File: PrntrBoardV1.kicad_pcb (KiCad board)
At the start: 4 copper layers, 99 x 99 mm, 234 parts, among them J1 EXT 5V, J10 Probe, J11 Extruder Heater, J12 Stepper, J13 Thermistor, J14 Max, J15 Min, J16 Max, J17 Min, J18 Max, J19 Min, J2 Bed Heater, J20 Stepper, J21 Stepper, J22 Stepper, J23 Stepper, J24 Probe, J25 Extruder Heater, J26 Stepper, J27 Thermistor, J28 Thermistor, J29 12-24V, J3 Z Probe, J30 LCD, J31 TC1, J32 TC2, J4 E0 Cool, J5 E0 Part, J6 E1 Cool, J7 E1 Part, J8 Always On Fan 1, J9 Always On Fan 2, U1 4078, U11 NUCLEO-64, U2 74HCT02, U3 74LVC125, U4 TMC5130, U5 TMC5130, U6 TMC5130, U7 TMC5130, U8 TMC5130, X1 16MHz

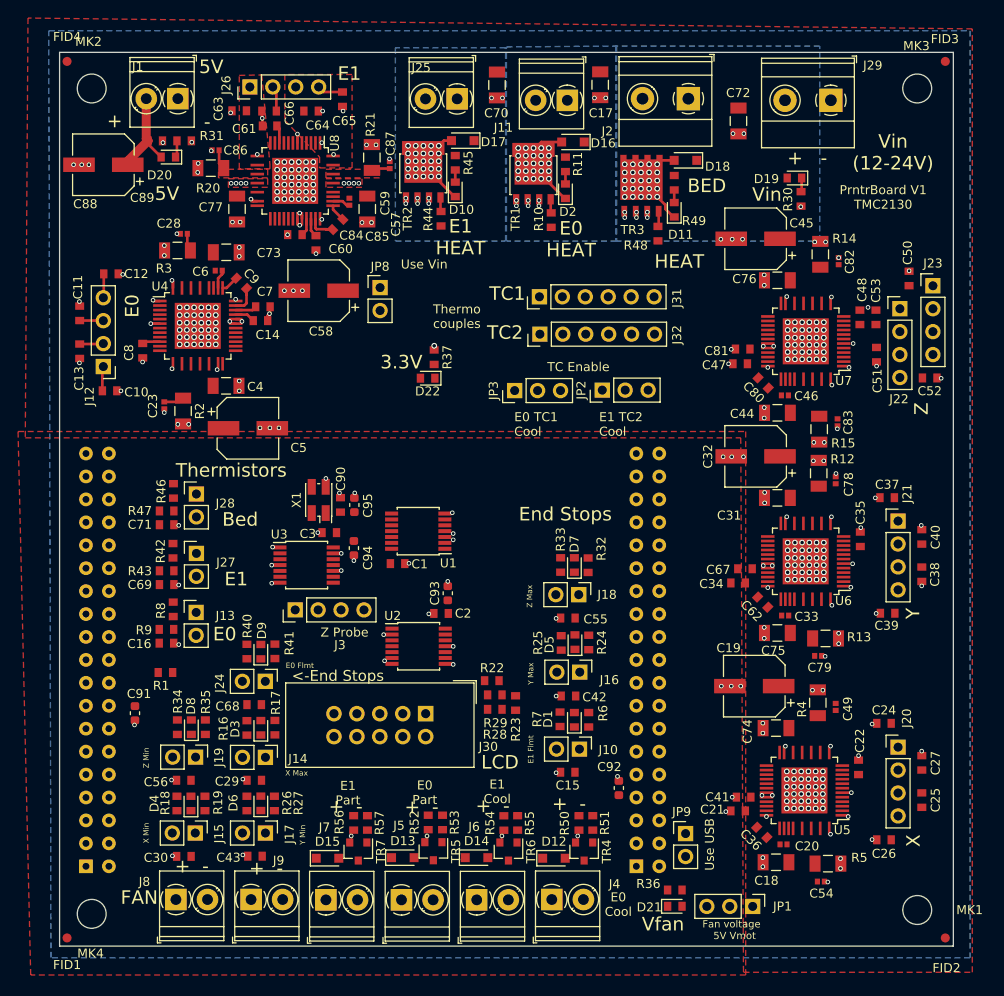
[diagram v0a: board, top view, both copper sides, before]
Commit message: Fix endstops. Add extra fan connectors. Start routing motors drivers.
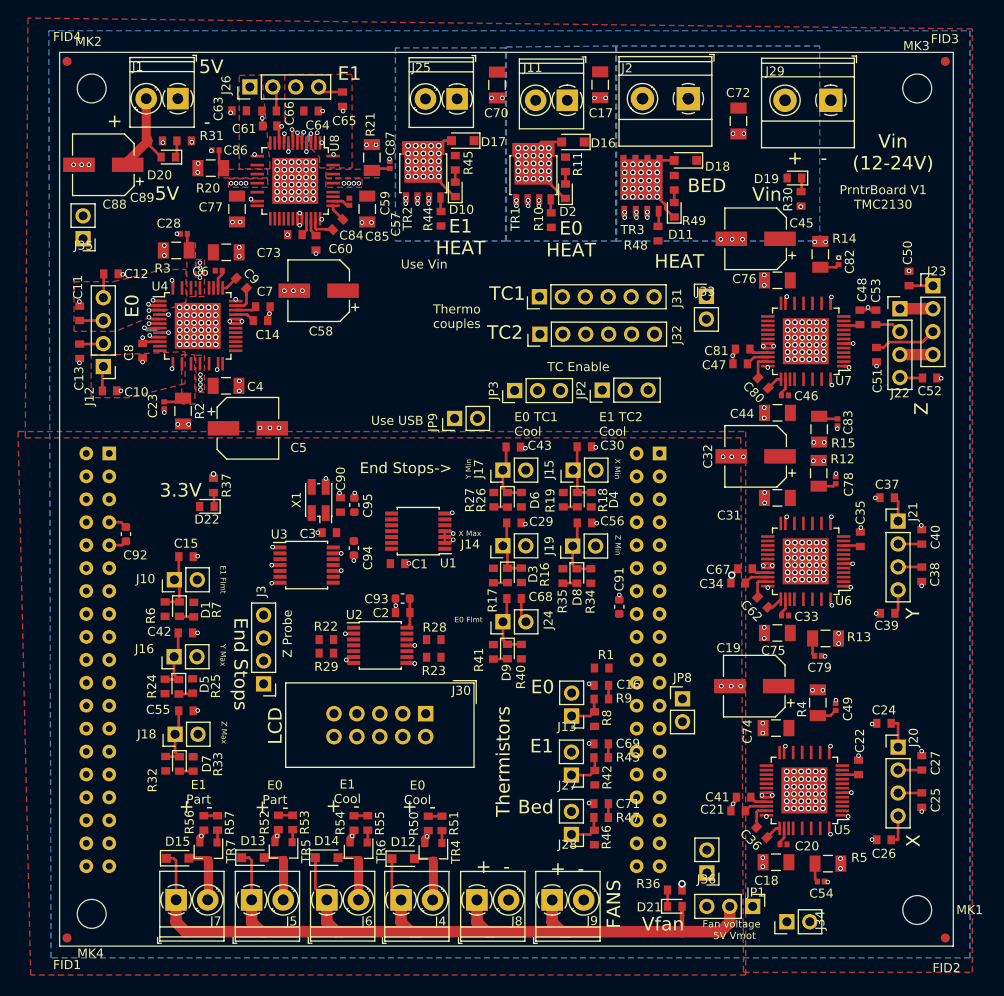
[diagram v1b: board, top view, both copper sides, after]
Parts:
- added J33: Vin, Connector_PinHeader_2.54mm:PinHeader_1x02_P2.54mm_Vertical, F.Cu at (91.7, 46.0)
- added J34: Vin, Connector_PinHeader_2.54mm:PinHeader_1x02_P2.54mm_Vertical, F.Cu at (100.6, 115.3)
- added J35: 5V, Connector_PinHeader_2.54mm:PinHeader_1x02_P2.54mm_Vertical, F.Cu at (22.6, 39.6)
- added J36: 5V, Connector_PinHeader_2.54mm:PinHeader_1x02_P2.54mm_Vertical, F.Cu at (91.7, 109.9)
- moved U11 78.3 mm to (86.5, 109.2), turned to 180 degrees
- moved C30 63.5 mm to (78.1, 62.7), turned to 0 degrees
- moved C92 61.4 mm to (27.4, 72.4), turned to 270 degrees
- moved R46 60.4 mm to (79.2, 106.0), turned to 90 degrees
- moved R47 58.9 mm to (80.0, 103.8), turned to 180 degrees
- moved J15 58.0 mm to (76.9, 65.3), turned to 90 degrees
- moved C71 57.2 mm to (80.0, 102.2), turned to 180 degrees
- moved R18 56.9 mm to (78.9, 68.5), turned to 90 degrees
- moved JP8 56.5 mm to (89.0, 90.6)
- moved J28 56.1 mm to (76.7, 105.6), turned to 180 degrees
- moved C91 54.9 mm to (82.0, 80.4), turned to 90 degrees
- moved D4 54.4 mm to (77.3, 68.5), turned to 270 degrees
- moved C43 53.6 mm to (70.3, 62.7), turned to 0 degrees
- moved R42 53.1 mm to (79.3, 99.3), turned to 90 degrees
- moved C56 52.8 mm to (78.1, 71.1), turned to 0 degrees
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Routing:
- net /E0 Cooling Fan/V_FAN: track 0.00 -> 114.2 mm
- net GND: track 14.9 -> 77.9 mm
- net /3.3V: track 3.98 -> 30.0 mm, vias 0 -> 2
- net /MISO: track 0.00 -> 23.8 mm, vias 0 -> 2
- net /MOSI_BUF: track 0.00 -> 20.7 mm, vias 0 -> 2
- net /MotorControl/E0/CLOCK: track 0.00 -> 19.6 mm, vias 0 -> 2
- net /SCK_BUF: track 0.00 -> 15.5 mm, vias 0 -> 2
- net /5V: track 15.2 -> 26.5 mm
- net /~E1_CS: track 0.00 -> 11.1 mm, vias 0 -> 1
- net /E0_DIR: track 0.00 -> 10.6 mm, vias 0 -> 1
- net /~E0_CS: track 0.00 -> 10.2 mm, vias 0 -> 1
- net /E1_DIR: track 0.00 -> 9.49 mm, vias 0 -> 1
- net /E1_STEP: track 0.00 -> 8.69 mm, vias 0 -> 1
- net /E0_STEP: track 0.00 -> 8.57 mm, vias 0 -> 1
- net /MotorControl/Y Axis/MaxStop/SENSOR: track 0.00 -> 7.12 mm
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- added copper zone on F.Cu, net /MotorControl/E0/Driver/MOTA1
- added copper zone on F.Cu, net /MotorControl/E0/Driver/MOTA2
- added copper zone on In2.Cu, net /MotorControl/E0/Driver/MOTA2
- added copper zone on F.Cu, net /MotorControl/E0/Driver/MOTB1
- added copper zone on F.Cu, net /MotorControl/E0/Driver/MOTB2
- added copper zone on In2.Cu, net /MotorControl/E0/Driver/MOTB2
- added copper zone on F.Cu, net Net-(C23-Pad1)
- added copper zone on F.Cu, net Net-(C28-Pad1)
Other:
- board text added: "End Stops->"
- board text added: "FANS"
- board text removed: "<-End Stops"
- board text removed: "FAN"

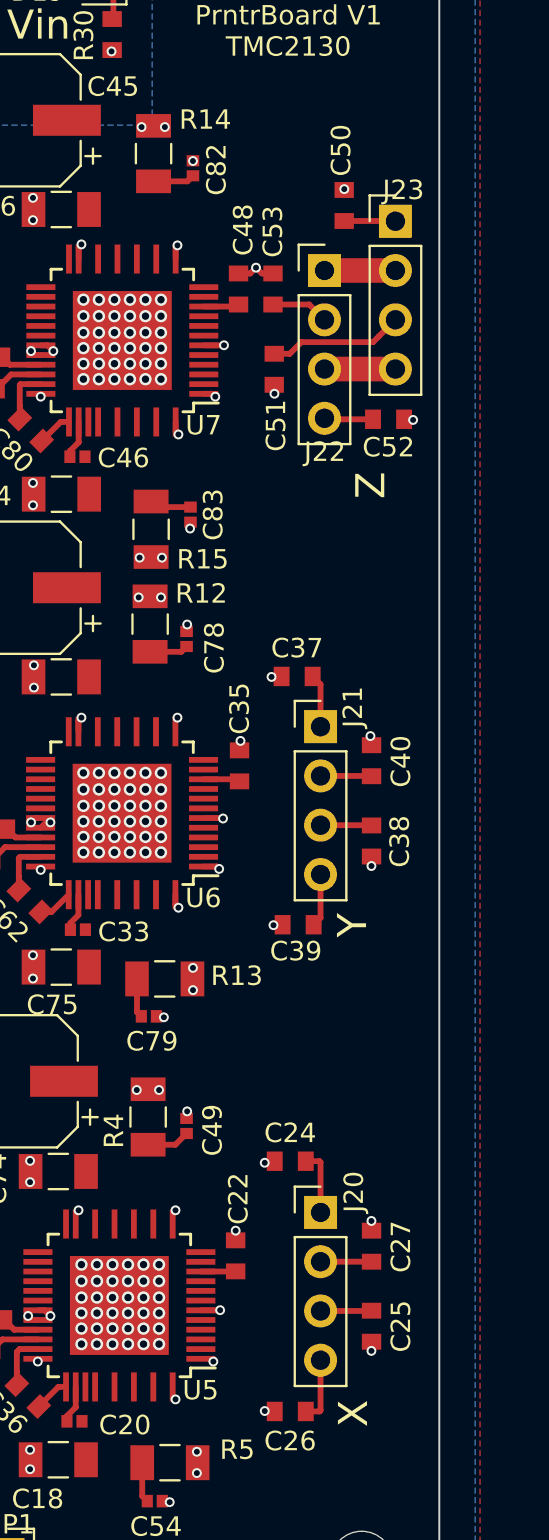
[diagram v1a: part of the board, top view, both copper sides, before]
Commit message: Added more motor power traces.
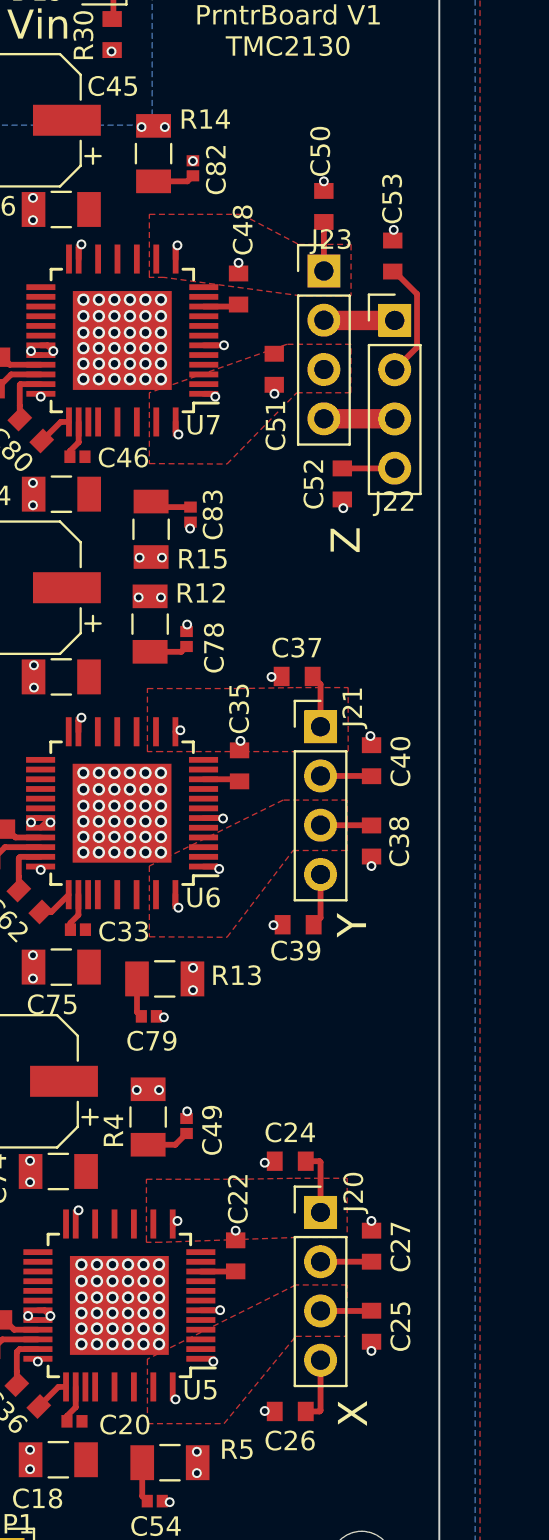
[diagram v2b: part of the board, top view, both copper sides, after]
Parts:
- moved C53 6.40 mm to (116.6, 46.6)
- moved J23 4.49 mm to (113.0, 47.4)
- moved J22 4.44 mm to (116.7, 50.0)
- moved C52 4.10 mm to (114.0, 58.4), turned to 90 degrees
- moved C50 1.05 mm to (113.0, 44.1)
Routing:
- net /MotorControl/Z Axis/MOTA1: track 6.97 -> 0.00 mm
- net /MotorControl/Z Axis/MOTB2: track 2.98 -> 6.11 mm
- net GND: track 77.9 -> 78.1 mm, vias 380 -> 381
- added copper zone on F.Cu, net /MotorControl/X Axis/MOTA1
- added copper zone on F.Cu, net /MotorControl/X Axis/MOTB1
- added copper zone on F.Cu, net /MotorControl/Y Axis/MOTA1
- added copper zone on F.Cu, net /MotorControl/Y Axis/MOTB1
- added copper zone on F.Cu, net /MotorControl/Z Axis/MOTA1
- added copper zone on F.Cu, net /MotorControl/Z Axis/MOTB1

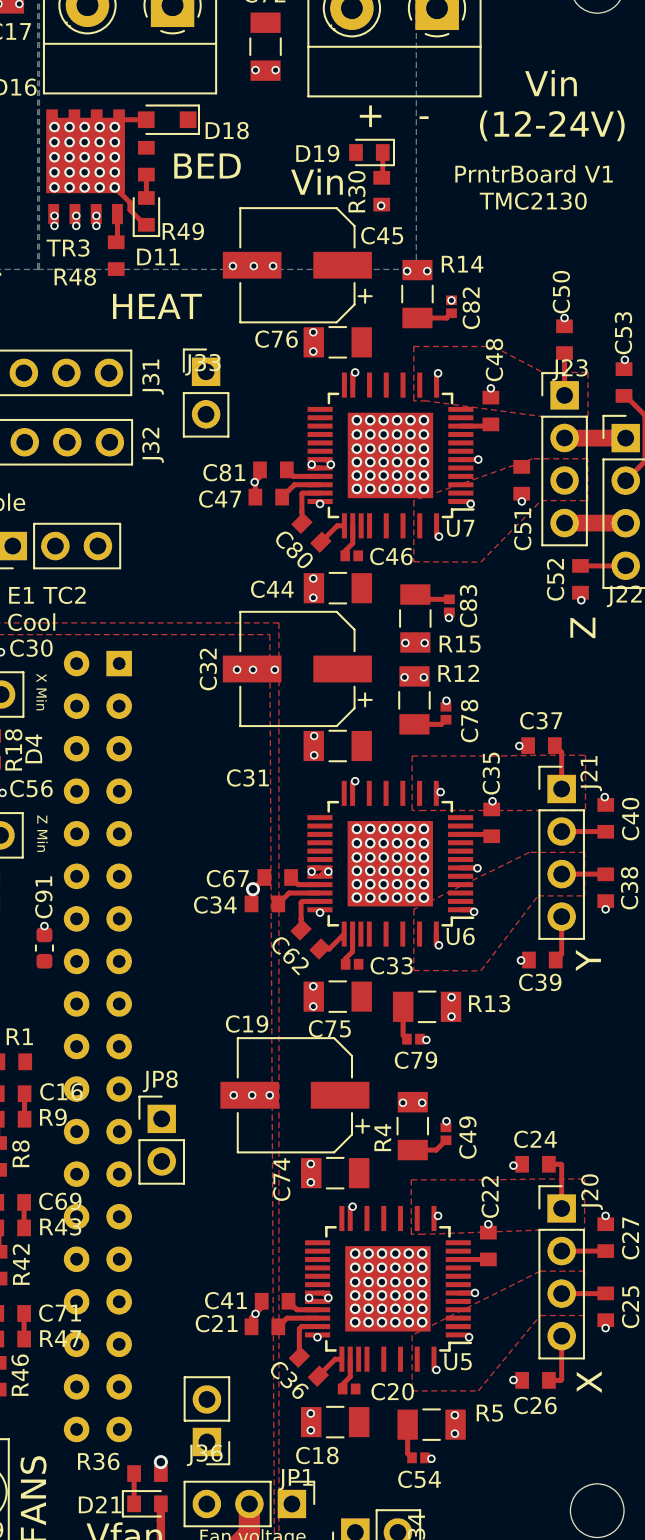
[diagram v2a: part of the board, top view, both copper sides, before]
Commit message: Routed all motor driver power traces.
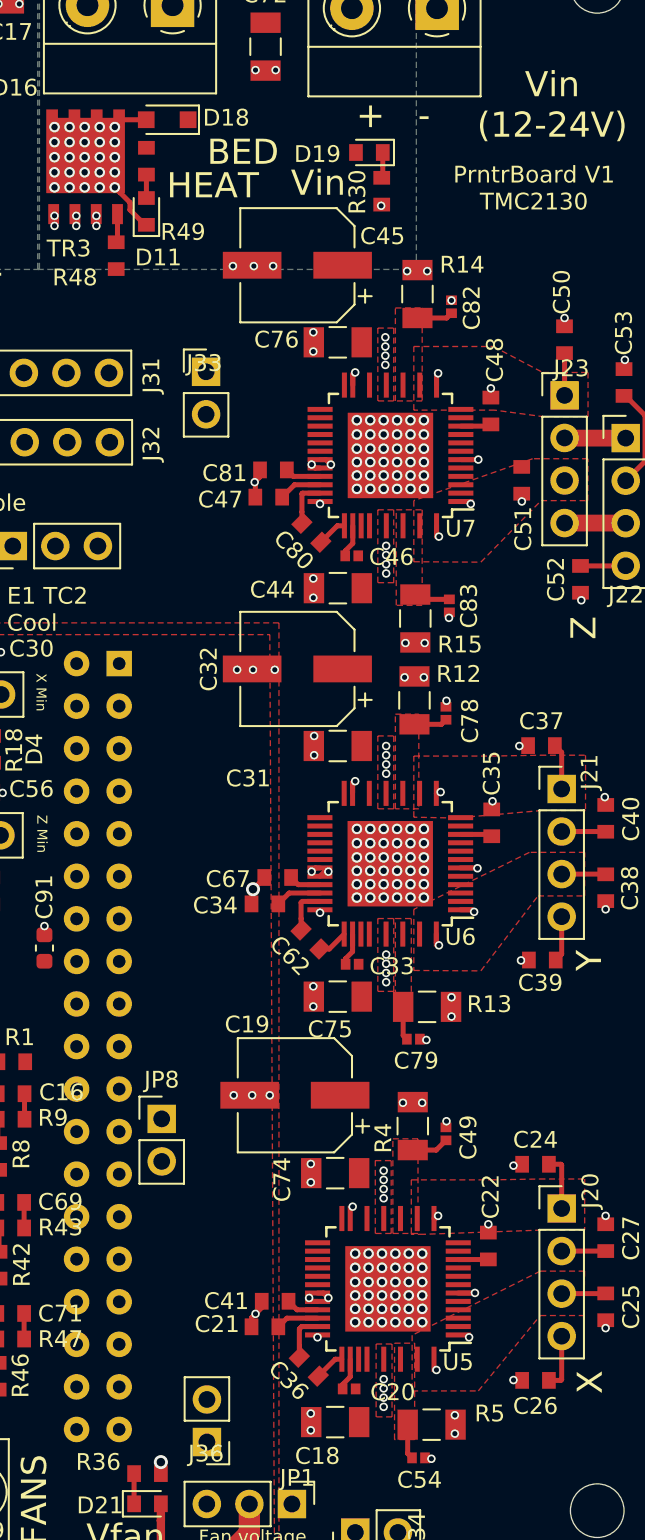
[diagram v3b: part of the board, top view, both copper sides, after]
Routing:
- net /MotorControl/Z Axis/MOTB2: vias 0 -> 4
- net /MotorControl/Z Axis/MOTA2: vias 0 -> 4
- net /MotorControl/Y Axis/MOTB2: vias 0 -> 4
- net /MotorControl/Y Axis/MOTA2: vias 0 -> 4
- net /MotorControl/X Axis/MOTB2: vias 0 -> 4
- net /MotorControl/X Axis/MOTA2: vias 0 -> 4
- added copper zone on F.Cu, net /MotorControl/X Axis/MOTA2
- added copper zone on In2.Cu, net /MotorControl/X Axis/MOTA2
- added copper zone on F.Cu, net /MotorControl/X Axis/MOTB2
- added copper zone on In2.Cu, net /MotorControl/X Axis/MOTB2
- added copper zone on F.Cu, net /MotorControl/Y Axis/MOTA2
- added copper zone on In2.Cu, net /MotorControl/Y Axis/MOTA2
- added copper zone on F.Cu, net /MotorControl/Y Axis/MOTB2
- added copper zone on In2.Cu, net /MotorControl/Y Axis/MOTB2
- added copper zone on F.Cu, net /MotorControl/Z Axis/MOTA2
- added copper zone on In2.Cu, net /MotorControl/Z Axis/MOTA2
- added copper zone on F.Cu, net /MotorControl/Z Axis/MOTB2
- added copper zone on In2.Cu, net /MotorControl/Z Axis/MOTB2
- added copper zone on F.Cu, net Net-(C49-Pad1)
- added copper zone on F.Cu, net Net-(C54-Pad1)
- added copper zone on F.Cu, net Net-(C78-Pad1)
- added copper zone on F.Cu, net Net-(C79-Pad1)
- added copper zone on F.Cu, net Net-(C82-Pad1)
- added copper zone on F.Cu, net Net-(C83-Pad1)

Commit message: 59 traces to go.
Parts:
- moved J35 2.71 mm to (22.9, 37.0), turned to 0 degrees
- moved C85 1.14 mm to (46.8, 40.1), turned to 90 degrees
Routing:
- net /MISO: track 23.8 -> 219.2 mm, vias 2 -> 9
- net /MOSI_BUF: track 20.7 -> 207.0 mm, vias 2 -> 11
- net /MotorControl/E0/CLOCK: track 19.6 -> 203.9 mm, vias 2 -> 11
- net /SCK_BUF: track 15.5 -> 192.3 mm, vias 2 -> 11
- net /5V: track 26.5 -> 189.5 mm, vias 0 -> 7
- net /3.3V: track 30.0 -> 171.9 mm, vias 2 -> 11
- net /MotorControl/E0/~ENABLE: track 0.00 -> 105.6 mm, vias 0 -> 10
- net /E0_DIR: track 10.6 -> 39.0 mm
- net /X_STEP: track 0.00 -> 26.8 mm, vias 0 -> 1
- net /AVREF: track 2.07 -> 27.6 mm
- net /Z_DIR: track 0.00 -> 24.6 mm, vias 0 -> 1
- net /~Z_CS: track 0.00 -> 23.1 mm, vias 0 -> 1
- net /Y_DIR: track 0.00 -> 23.0 mm, vias 0 -> 1
- net /Z_STEP: track 0.00 -> 22.7 mm, vias 0 -> 1
- net /~Y_CS: track 0.00 -> 22.1 mm, vias 0 -> 1
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
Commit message: 39 Traces to go.
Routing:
- net /~Z_CS: track 23.1 -> 107.1 mm, vias 1 -> 3
- net /Heated Bed/PWM: track 0.00 -> 78.7 mm, vias 0 -> 5
- net /E1_DIR: track 27.8 -> 101.3 mm, vias 1 -> 3
- net /MotorControl/E0/~ENABLE: track 105.6 -> 176.9 mm, vias 10 -> 15
- net /E0_STEP: track 18.0 -> 80.9 mm, vias 1 -> 3
- net /E0_PWM: track 0.00 -> 62.5 mm, vias 0 -> 3
- net /E0_COOL_TC1: track 0.00 -> 61.9 mm, vias 0 -> 2
- net /~E1_CS: track 21.8 -> 79.1 mm, vias 1 -> 3
- net /E1_STEP: track 26.5 -> 75.1 mm, vias 1 -> 3
- net /E1_PWM: track 0.00 -> 48.4 mm, vias 0 -> 2
- net /~E0_CS: track 29.2 -> 74.5 mm, vias 1 -> 3
- net /5V: track 189.5 -> 228.9 mm, vias 7 -> 9
- net /MotorControl/E0/CLOCK: track 203.9 -> 242.4 mm, vias 11 -> 13
- net /MotorControl/E1_SG: track 15.2 -> 51.4 mm, vias 1 -> 5
- net /E0_PART_PWM: track 1.59 -> 37.7 mm, vias 0 -> 2
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
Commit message: All routed :-)))
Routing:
- net /5V: track 228.9 -> 105.9 mm, vias 9 -> 7
- net /Z_STEP: track 32.0 -> 135.9 mm, vias 2 -> 5
- net /Z_DIR: track 35.8 -> 136.6 mm, vias 2 -> 5
- net /E1_COOL_TC2: track 0.00 -> 91.4 mm, vias 0 -> 3
- net /AVREF: track 27.6 -> 105.0 mm, vias 0 -> 2
- net /Y_DIR: track 23.0 -> 97.2 mm, vias 1 -> 3
- net /E1_COOL_PWM: track 1.53 -> 73.7 mm, vias 0 -> 2
- net /MOSI: track 0.00 -> 70.7 mm, vias 0 -> 3
- net /Y_STEP: track 20.4 -> 90.3 mm, vias 1 -> 3
- net /X_DIR: track 22.0 -> 91.7 mm, vias 1 -> 3
- net /~Y_CS: track 22.1 -> 87.9 mm
- net /~X_CS: track 21.8 -> 85.1 mm
- net /MOSI_BUF: track 207.9 -> 270.7 mm, vias 13 -> 16
- net /MotorControl/X_SG: track 10.1 -> 68.4 mm, vias 1 -> 5
- net /Z_PROBE_MOD: track 2.23 -> 60.1 mm, vias 0 -> 3
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- added copper zone on In2.Cu, net /5V
- added copper zone on In2.Cu, net /Heated Bed/HEATER
- added copper zone on In2.Cu, net /MotorControl/E0/Heating/HEATER
- added copper zone on In2.Cu, net /MotorControl/E1/Heating/HEATER

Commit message: Cleanup. Generated gerbers.
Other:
- board text added: "(c) iQury.us July 2018"
- board text removed: "(c) iQury.us May 2018"
